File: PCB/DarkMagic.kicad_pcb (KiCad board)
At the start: 6 copper layers, 157 x 73 mm, 212 parts, among them IC1 5PB1106PGGI8, IC10 MMBT3904-AQ, IC11 MMBT3904-AQ, IC12 SN74LVC1G125DBVT, IC13 SN74LVC1G125DBVT, IC14 LM3940IMP-3.3_NOPB, IC15 SN74LVC1G125DBVT, IC17 LM393DR, IC2 ESP32-WROOM-32UE-N16, IC3 MMBT3904-AQ, IC4 MMBT3904-AQ, IC5 W5500, IC6 CP2102N-A02-GQFN24, IC7 USBLC6-2SC6, IC8 LMR33640ADDAR, J1 USB_C_Receptacle_USB2.0_16P, J2 TMJ0026ABNL, J3 5747842-2, J4 Screw_Terminal_01x02, J5 Screw_Terminal_01x02, J6 5747842-2, J7 171825-2, J9 Conn_01x04, Q1 SQ2319ADS-T1_BE3, Q2 SQ2348ES-T1_BE3, U1 SC16IS752IPW_128, U2 SC16IS752IPW_128, U3 CD74HC138QM96Q1, U4 SC16IS752IPW_128, U5 SC16IS752IPW_128, U6 SC16IS752IPW_128, U7 SC16IS752IPW_128, Y2 ASE-14.7456MHZ-LC-T, Y3 ASE-25.000MHZ-LC-T

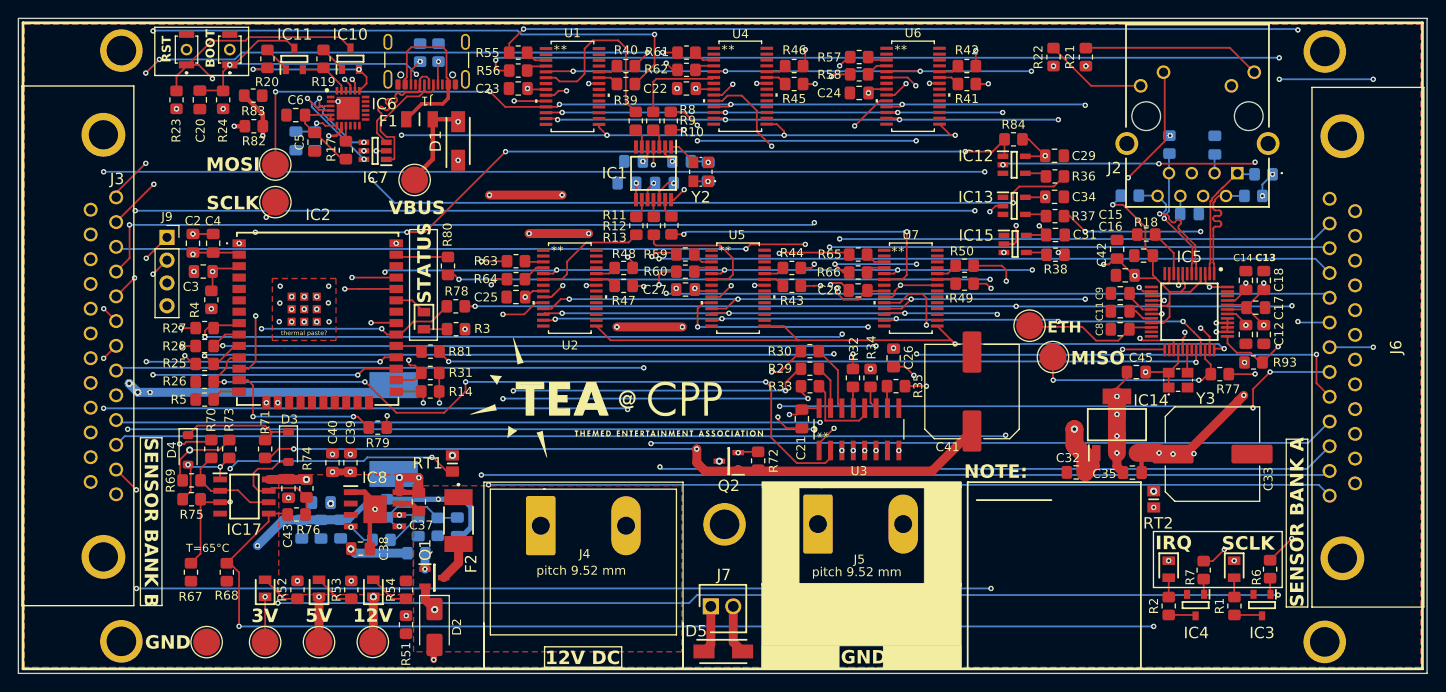
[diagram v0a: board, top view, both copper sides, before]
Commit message: The W5500 actually works, I just wired it wrong
Pulled back some pins and it's working now! Fixed this error in schematic, code was updated to reflect this
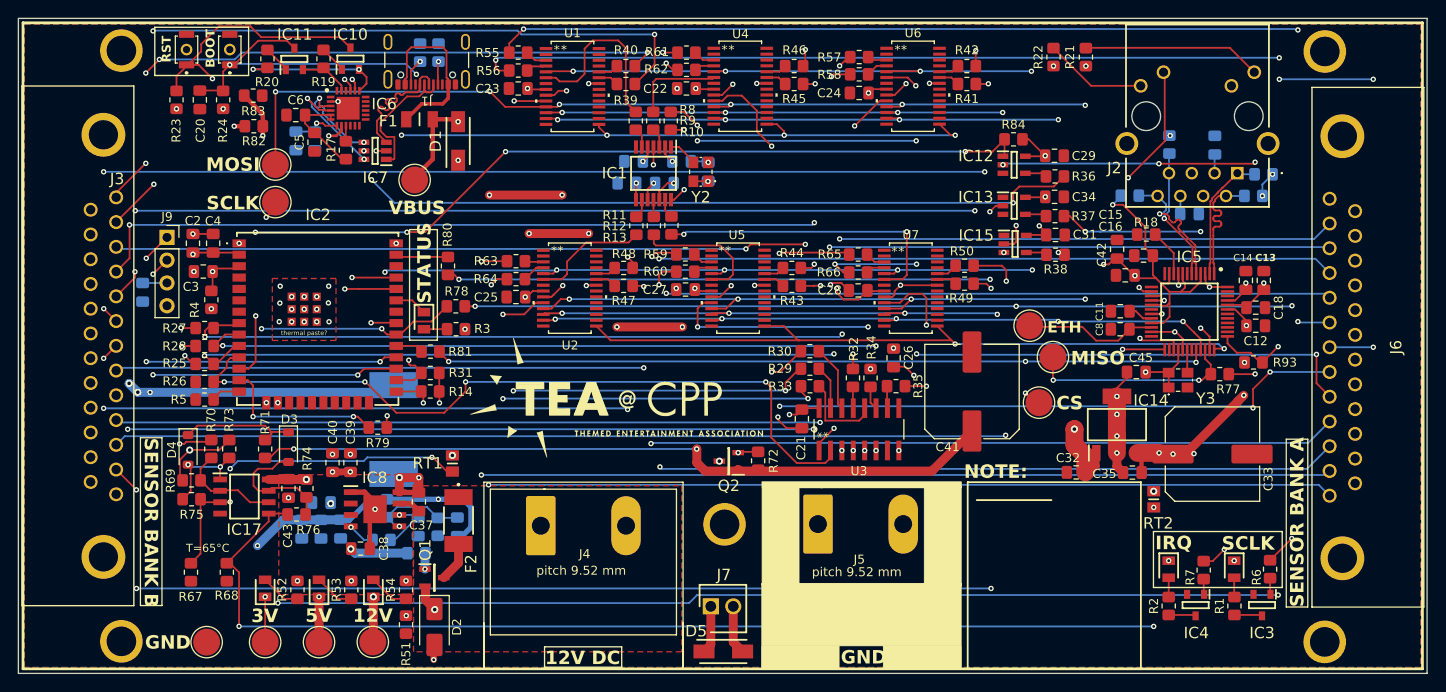
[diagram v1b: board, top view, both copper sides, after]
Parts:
- removed C9: 0.1uF, Capacitor_SMD:C_0805_2012Metric_Pad1.18x1.45mm_HandSolder
- added TP10: TestPoint, TestPoint:TestPoint_Pad_D3.0mm, F.Cu at (189.5, 64.7)
- C11: value 10nF -> 4.7uF
- C17: moved to B.Cu
- moved C17 123.0 mm to (89.6, 52.4)
- moved C12 1.32 mm to (213.7, 56.2), turned to 0 degrees
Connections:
- IC5 pad 18: /VBG -> unconnected-(IC5-VBG-Pad18)
- IC5 pad 23: unconnected-(IC5-RSVD_1-Pad23) -> GND
- IC5 pad 38: GND -> unconnected-(IC5-RSVD_2-Pad38)
- IC5 pad 39: GND -> unconnected-(IC5-RSVD_3-Pad39)
- IC5 pad 40: GND -> unconnected-(IC5-RSVD_4-Pad40)
- IC5 pad 41: GND -> unconnected-(IC5-RSVD_5-Pad41)
- IC5 pad 42: +3V3 -> unconnected-(IC5-RSVD_6-Pad42)
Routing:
- net /ESP_SCSN: track 86.2 -> 91.7 mm, vias 2 -> 4
- net /VBG: track 3.04 -> 0.00 mm
- net /ESP_EN: track 52.4 -> 53.9 mm
- net +3V3: track 217.5 -> 216.1 mm, vias 48 -> 47
- net GND: track 86.7 -> 85.7 mm, vias 70 -> 69
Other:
- board text added: "CS"
